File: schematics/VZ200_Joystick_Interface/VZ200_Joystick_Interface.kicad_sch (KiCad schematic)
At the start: 25 parts, among them J1 Right Joystick, J2 Left Joystick, P1 I/O Expansion, U1 74LS08, U2 74LS138, U3 74LS365

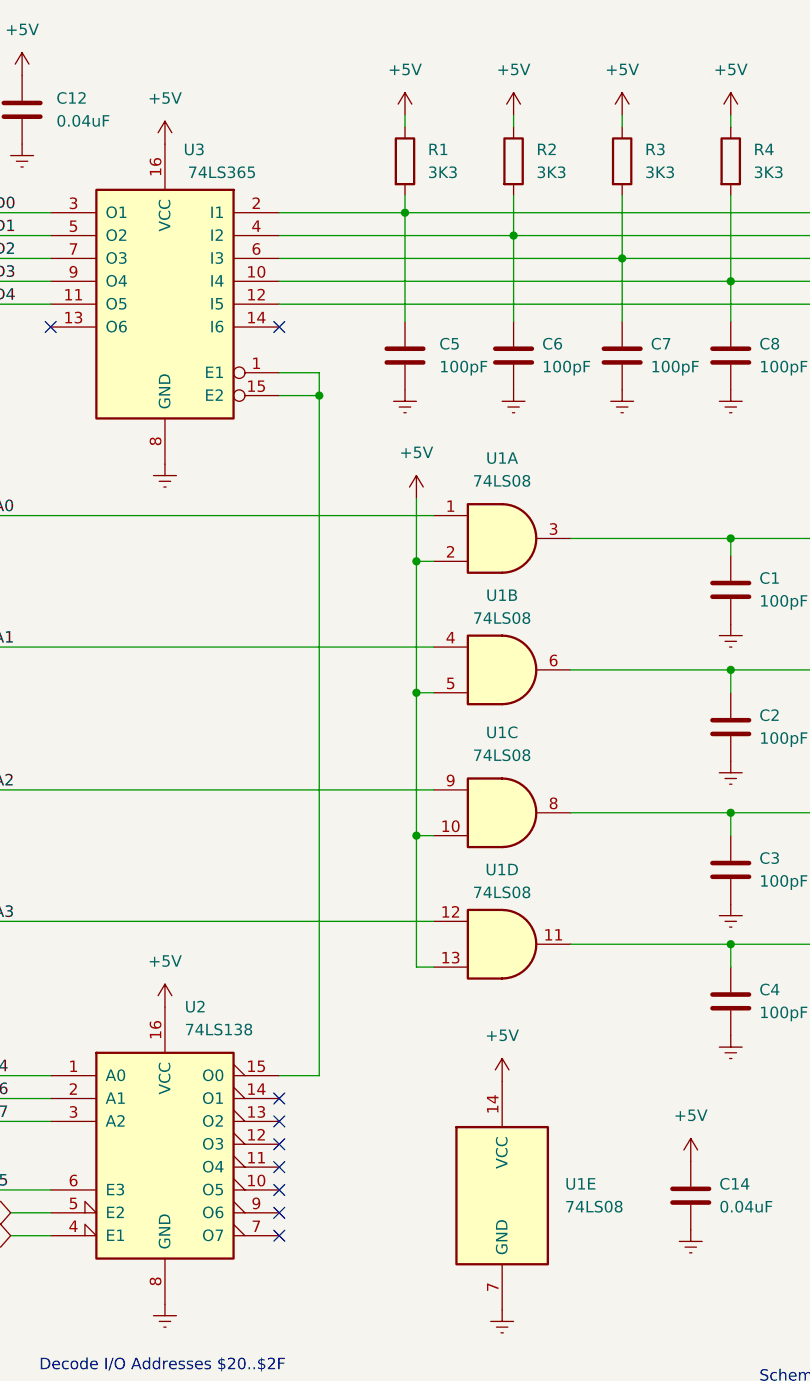
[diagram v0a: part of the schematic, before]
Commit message: Update part numbers for the joystick interface
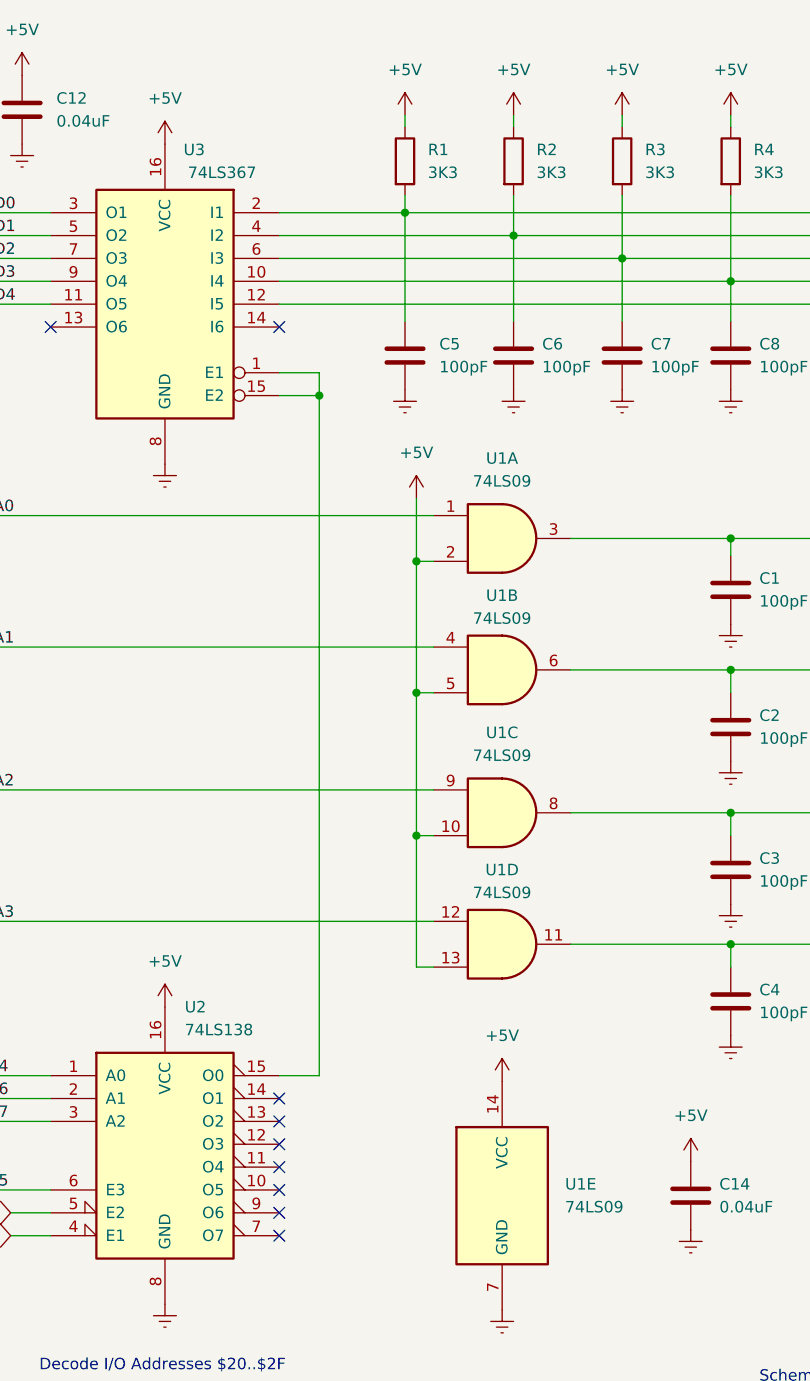
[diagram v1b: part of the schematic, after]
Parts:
- U1: value 74LS08 -> 74LS09
- U3: value 74LS365 -> 74LS367
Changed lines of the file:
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@@
       (effects (font (size 1.27 1.27)) (justify left))
     )
-    (property "Value" "74LS365" (at 127.635 40.64 0)
+    (property "Value" "74LS367" (at 127.635 40.64 0)
       (effects (font (size 1.27 1.27)) (justify left))
     )
@@
       (effects (font (size 1.27 1.27)))
     )
-    (property "Value" "74LS08" (at 154.9317 90.17 0)
+    (property "Value" "74LS09" (at 154.9317 90.17 0)
       (effects (font (size 1.27 1.27)))
     )
@@
       (effects (font (size 1.27 1.27)) hide)
     )
-    (property "Datasheet" "http://www.ti.com/lit/gpn/sn74LS08" (at 154.94 95.885 0)
+    (property "Datasheet" "http://www.ti.com/lit/gpn/sn74LS09" (at 154.94 95.885 0)
       (effects (font (size 1.27 1.27)) hide)
     )
@@
       (effects (font (size 1.27 1.27)) (justify left))
     )
-    (property "Value" "74LS08" (at 161.925 155.575 0)
+    (property "Value" "74LS09" (at 161.925 155.575 0)
       (effects (font (size 1.27 1.27)) (justify left))
     )
@@
       (effects (font (size 1.27 1.27)) hide)
     )
-    (property "Datasheet" "http://www.ti.com/lit/gpn/sn74LS08" (at 154.94 154.305 0)
+    (property "Datasheet" "http://www.ti.com/lit/gpn/sn74LS09" (at 154.94 154.305 0)
       (effects (font (size 1.27 1.27)) hide)
     )
@@
       (effects (font (size 1.27 1.27)))
     )
-    (property "Value" "74LS08" (at 154.9317 105.41 0)
+    (property "Value" "74LS09" (at 154.9317 105.41 0)
       (effects (font (size 1.27 1.27)))
     )
@@
       (effects (font (size 1.27 1.27)) hide)
     )
-    (property "Datasheet" "http://www.ti.com/lit/gpn/sn74LS08" (at 154.94 111.76 0)
+    (property "Datasheet" "http://www.ti.com/lit/gpn/sn74LS09" (at 154.94 111.76 0)
       (effects (font (size 1.27 1.27)) hide)
     )
@@
       (effects (font (size 1.27 1.27)))
     )
-    (property "Value" "74LS08" (at 154.9317 120.65 0)
+    (property "Value" "74LS09" (at 154.9317 120.65 0)
       (effects (font (size 1.27 1.27)))
     )
@@
       (effects (font (size 1.27 1.27)) hide)
     )
-    (property "Datasheet" "http://www.ti.com/lit/gpn/sn74LS08" (at 154.94 126.365 0)
+    (property "Datasheet" "http://www.ti.com/lit/gpn/sn74LS09" (at 154.94 126.365 0)
       (effects (font (size 1.27 1.27)) hide)
     )
@@
       (effects (font (size 1.27 1.27)))
     )
-    (property "Value" "74LS08" (at 154.9317 74.93 0)
+    (property "Value" "74LS09" (at 154.9317 74.93 0)
       (effects (font (size 1.27 1.27)))
     )
@@
       (effects (font (size 1.27 1.27)) hide)
     )
-    (property "Datasheet" "http://www.ti.com/lit/gpn/sn74LS08" (at 154.94 81.28 0)
-      (effects (font (size 1.27 1.27)) hide)
-    )
+    (property "Datasheet" "http://www.ti.com/lit/gpn/sn74LS09" (at 154.94 81.28 0)
+      (effects (font (size 1.27 1.27)) hide)
+    )
